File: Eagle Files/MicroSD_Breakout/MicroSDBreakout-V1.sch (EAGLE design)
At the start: 2 parts

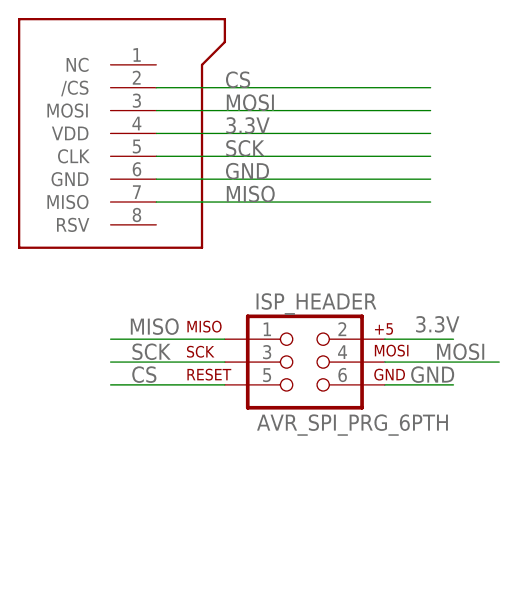
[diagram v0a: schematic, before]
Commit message: MicroSD Breakout Board now has a pull up resistor on CS
--Arthur

git-svn-id: http://cd-net.net/CPE496/trunk@89 05b6d0e0-c345-4a8e-a5b7-579c8bd0b646
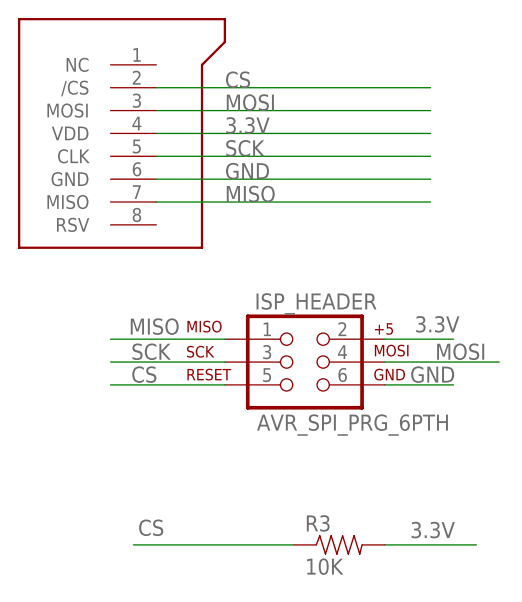
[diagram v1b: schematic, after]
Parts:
- added R3: 10K, SparkFun:RESISTOR0603-RES
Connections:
- net 3.3V: now also R3.2
- net CS: now also R3.1
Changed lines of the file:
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@@
 <part name="U$1" library="group10" deviceset="MICROSD" device=""/>
 <part name="ISP_HEADER" library="SparkFun" deviceset="AVR_SPI_PRG_6" device="PTH"/>
+<part name="R3" library="SparkFun" deviceset="RESISTOR" device="0603-RES" value="10K"/>
 </parts>
 <sheets>
@@
 <instance part="U$1" gate="G$1" x="63.5" y="53.34" rot="R270"/>
 <instance part="ISP_HEADER" gate="G$1" x="86.36" y="27.94"/>
+<instance part="R3" gate="G$1" x="91.44" y="7.62"/>
 </instances>
 <busses>
@@
 <label x="78.74" y="53.34" size="1.778" layer="95"/>
 </segment>
+<segment>
+<pinref part="R3" gate="G$1" pin="2"/>
+<wire x1="96.52" y1="7.62" x2="106.68" y2="7.62" width="0.1524" layer="91"/>
+<label x="99.314" y="8.382" size="1.778" layer="95"/>
+</segment>
 </net>
 <net name="SCK" class="0">
@@
 <label x="78.74" y="58.42" size="1.778" layer="95"/>
 </segment>
+<segment>
+<pinref part="R3" gate="G$1" pin="1"/>
+<wire x1="86.36" y1="7.62" x2="68.58" y2="7.62" width="0.1524" layer="91"/>
+<label x="69.088" y="8.636" size="1.778" layer="95"/>
+</segment>
 </net>

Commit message: Main Board with Headers is now almost ready.
I'm adding the FTDI Module right now.

TODO:
1.  Double check regulator Datasheet.  I think we're missing a capacitor.
2.  Update Radio Module Schematics to incorporate ground plane.
3.  Check if the hall effect sensor can work linearly at 3.3V
4.  Finish Adding FTDI chip and USB connector.

--Arthur

git-svn-id: http://cd-net.net/CPE496/trunk@119 05b6d0e0-c345-4a8e-a5b7-579c8bd0b646
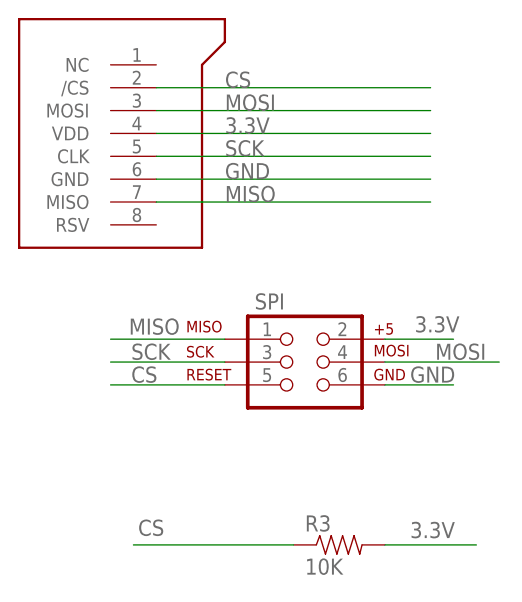
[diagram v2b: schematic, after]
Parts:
- renumbered ISP_HEADER to SPI
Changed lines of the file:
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@@
 </variantdefs>
 <classes>
-<class number="0" name="default" width="0.508" drill="0">
+<class number="0" name="default" width="0" drill="0">
 </class>
 </classes>
 <parts>
 <part name="U$1" library="group10" deviceset="MICROSD" device=""/>
-<part name="ISP_HEADER" library="SparkFun" deviceset="AVR_SPI_PRG_6" device="PTH"/>
+<part name="SPI" library="SparkFun" deviceset="AVR_SPI_PRG_6" device="PTH" value=""/>
 <part name="R3" library="SparkFun" deviceset="RESISTOR" device="0603-RES" value="10K"/>
 </parts>
@@
 <instances>
 <instance part="U$1" gate="G$1" x="63.5" y="53.34" rot="R270"/>
-<instance part="ISP_HEADER" gate="G$1" x="86.36" y="27.94"/>
+<instance part="SPI" gate="G$1" x="86.36" y="27.94"/>
 <instance part="R3" gate="G$1" x="91.44" y="7.62"/>
 </instances>
@@
 <net name="GND" class="0">
 <segment>
-<pinref part="ISP_HEADER" gate="G$1" pin="6"/>
+<pinref part="SPI" gate="G$1" pin="6"/>
 <wire x1="96.52" y1="25.4" x2="104.14" y2="25.4" width="0.1524" layer="91"/>
 <label x="99.314" y="25.654" size="1.778" layer="95"/>
@@
 <net name="MOSI" class="0">
 <segment>
-<pinref part="ISP_HEADER" gate="G$1" pin="4"/>
+<pinref part="SPI" gate="G$1" pin="4"/>
 <wire x1="96.52" y1="27.94" x2="109.22" y2="27.94" width="0.1524" layer="91"/>
 <label x="102.108" y="28.194" size="1.778" layer="95"/>
@@
 <net name="3.3V" class="0">
 <segment>
-<pinref part="ISP_HEADER" gate="G$1" pin="2"/>
+<pinref part="SPI" gate="G$1" pin="2"/>
 <wire x1="96.52" y1="30.48" x2="104.14" y2="30.48" width="0.1524" layer="91"/>
 <label x="99.822" y="31.242" size="1.778" layer="95"/>
@@
 <net name="SCK" class="0">
 <segment>
-<pinref part="ISP_HEADER" gate="G$1" pin="3"/>
+<pinref part="SPI" gate="G$1" pin="3"/>
 <wire x1="78.74" y1="27.94" x2="66.04" y2="27.94" width="0.1524" layer="91"/>
 <label x="68.326" y="28.194" size="1.778" layer="95"/>
@@
 <net name="MISO" class="0">
 <segment>
-<pinref part="ISP_HEADER" gate="G$1" pin="1"/>
+<pinref part="SPI" gate="G$1" pin="1"/>
 <wire x1="78.74" y1="30.48" x2="66.04" y2="30.48" width="0.1524" layer="91"/>
 <label x="68.072" y="30.988" size="1.778" layer="95"/>
@@
 <net name="CS" class="0">
 <segment>
-<pinref part="ISP_HEADER" gate="G$1" pin="5"/>
+<pinref part="SPI" gate="G$1" pin="5"/>
 <wire x1="78.74" y1="25.4" x2="66.04" y2="25.4" width="0.1524" layer="91"/>
 <label x="68.326" y="25.654" size="1.778" layer="95"/>
@@
 </sheet>
 </sheets>
-<errors>
-</errors>
 </schematic>
 </drawing>
